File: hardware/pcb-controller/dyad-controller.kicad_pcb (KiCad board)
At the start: 2 copper layers, 45.2 x 93.4 mm, 36 parts, among them J1 USB_C_Receptacle_USB2.0, J2 SWD, J3 Conn_01x11, J4 Conn_01x11, J5 Conn_01x11, SW1 SW_Push, U1 W25Q128JVS, U2 USBLC6-2SC6, U3 RP2040, U4 XC6206PxxxMR-Regulator_Linear, Y1 12MHz

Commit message: Sync the controller PCB with its schematic
The board still carried the upstream reference layout. Cleared its 433
tracks and 32 vias (routed for the 45 x 93 mm board and the old pin map)
and the J3/J4/J5 breakout headers, then added D1, F2, J6-J10 and SW2 from
the schematic, and swapped SW1 from a pin header to the TS-1187A button.

USB-C: the stock USB_C_Receptacle_USB2.0 symbol numbers its shield pin S1,
but KiCad 10's HRO TYPE-C-31-M-12 footprint names those pads SH, so J9/J10
could not be placed with their shield on GND. J1 only worked because it was
the KiCad 6 copy, which still said S1. Added dyad:USB_C_Receptacle_HRO_TYPE-
C-31-M-12 with the shield pads renumbered S1 and pointed J1, J9 and J10 at it.

SW1 fixes: Change Footprint netted only one pad of each duplicate-numbered
pair (the TS-1187A pads are 1,1,2,2), so all four are now netted by hand. It
was also excluded from the BOM -- in the schematic too, inherited from the
header -- which would have left the BOOTSEL button unfitted. Now in_bom yes,
value BOOTSEL.

Verified: 41/41 footprints and 41/41 footprint IDs match the schematic, and
all 246 schematic pins land on correctly netted pads. ERC unchanged at 152.
Parity leaves 14 field-copy differences (LCSC, Datasheet, Serves). The new
parts sit stacked off-board awaiting the 35 x 50 outline and placement.

Co-Authored-By: Claude Opus 5.5 <noreply@anthropic.com>
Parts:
- removed J3, J4, J5: Conn_01x11, Connector_PinSocket_2.54mm:PinSocket_1x11_P2.54mm_Vertical
- added D1: SS34, Diode_SMD:D_SMA, F.Cu at (8.50, 2.38)
- added F2: 500mA, Fuse:Fuse_1206_3216Metric, F.Cu at (7.28, 10.9)
- added J10: USB-C split link, dyad:USB_C_Receptacle_HRO_TYPE-C-31-M-12, F.Cu at (10.3, 70.1)
- added J6: HC-FPC-0.5-20P-FH20, dyad:FPC-SMD_20P-P0.50_HC-FPC-0.5-20P-FH20, F.Cu at (12.4, 20.1)
- added J7: HC-FPC-0.5-20P-FH20, dyad:FPC-SMD_20P-P0.50_HC-FPC-0.5-20P-FH20, F.Cu at (12.4, 31.4)
- added J8: HC-FPC-0.5-14P-FH20, dyad:FPC-SMD_14P-P0.50_HC-FPC-0.5-14P-FH20, F.Cu at (10.9, 42.7)
- added J9: USB-C split link, dyad:USB_C_Receptacle_HRO_TYPE-C-31-M-12, F.Cu at (10.3, 55.7)
- added SW2: RESET, Button_Switch_SMD:SW_Push_1P1T_XKB_TS-1187A, F.Cu at (8.75, 83.3)
- J1: footprint Connector_USB:USB_C_Receptacle_HRO_TYPE-C-31-M-12 -> dyad:USB_C_Receptacle_HRO_TYPE-C-31-M-12
- SW1: value SW_Push -> BOOTSEL; footprint Connector_PinSocket_2.54mm:PinSocket_1x02_P2.54mm_Vertical -> Button_Switch_SMD:SW_Push_1P1T_XKB_TS-1187A
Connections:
- F1 pad 2: +5V -> /VBUS_FUSED
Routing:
- net +3V3: track 75.2 -> 0.00 mm, vias 3 -> 0
- net /GPIO0: track 60.8 -> 0.00 mm
- net /GPIO10: track 57.6 -> 0.00 mm
- net /GPIO1: track 57.4 -> 0.00 mm
- net GND: track 56.8 -> 0.00 mm, vias 25 -> 0
- net /GPIO20: track 54.7 -> 0.00 mm
- net /GPIO11: track 54.3 -> 0.00 mm
- net /GPIO2: track 54.0 -> 0.00 mm
- net /GPIO21: track 52.7 -> 0.00 mm
- net /GPIO22: track 51.7 -> 0.00 mm
- net /GPIO12: track 51.6 -> 0.00 mm
- net /GPIO3: track 50.7 -> 0.00 mm
- net /GPIO23: track 49.7 -> 0.00 mm
- net /GPIO13: track 49.1 -> 0.00 mm
- net /GPIO24: track 47.6 -> 0.00 mm
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
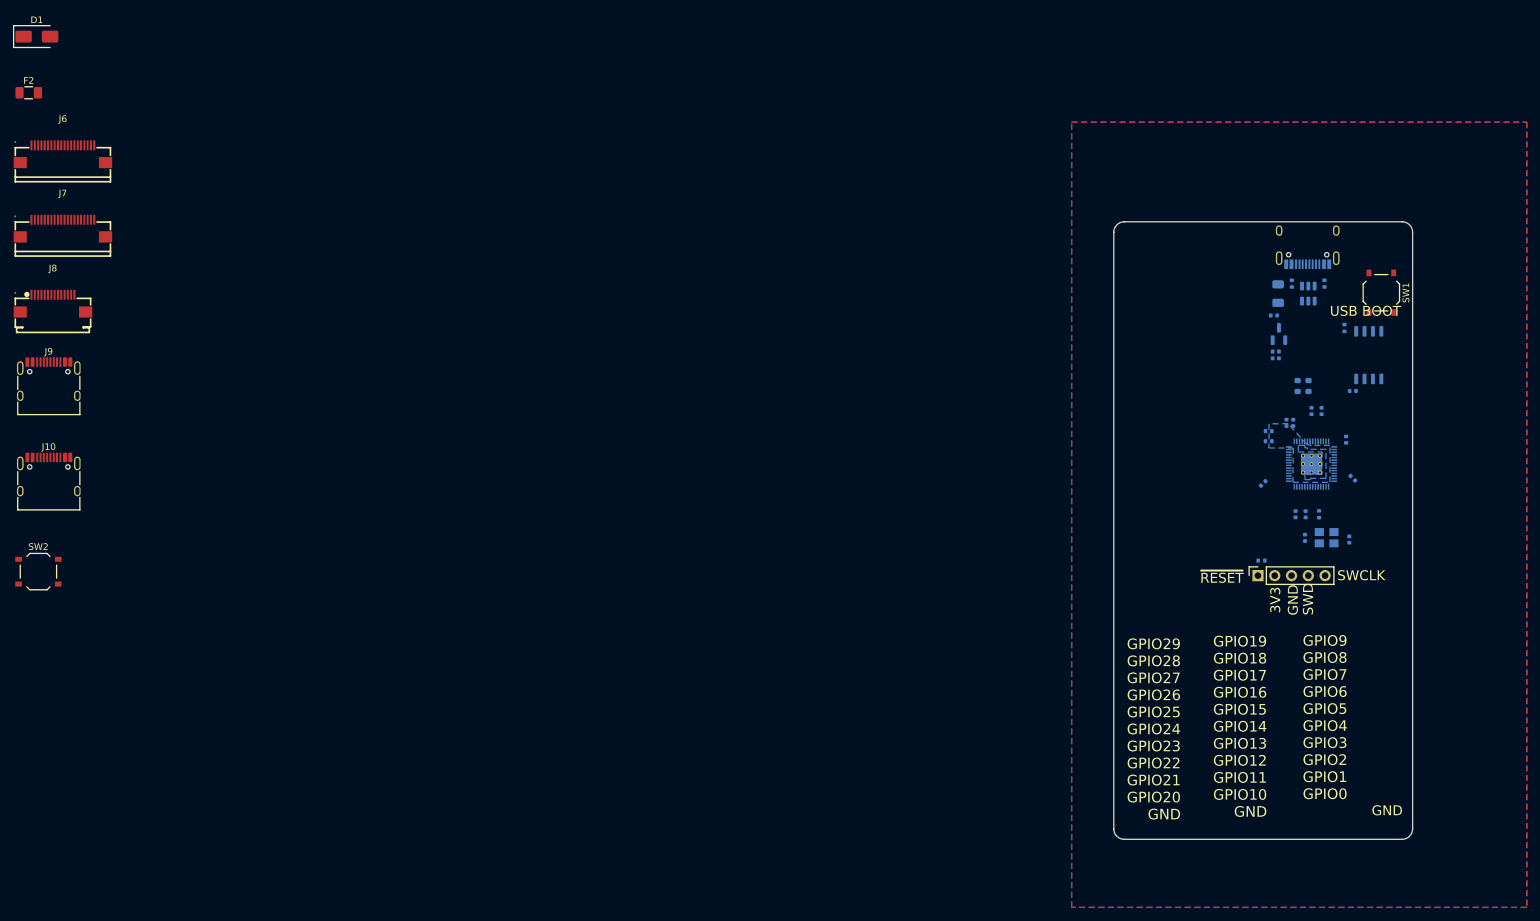
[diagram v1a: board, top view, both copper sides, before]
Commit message: Turn the controller outline to 35 x 50, place the edge connectors and M2 mounting holes
Outline: the upstream 45 x 93 mm shape replaced with 35 wide x 50 deep,
2 mm corners -- the interface.yaml envelope turned 90 degrees so the 50 mm
side edges carry the main FFC and split USB-C. Drawn around the existing
RP2040 so the upstream decoupling cluster stays where it is. The case DXF
and generate_controller_outline.py follow.

Edge connectors, all on B.Cu: J1 host USB-C on the rear; J6/J7 main FFC on
the left/right edges level with U3; J10/J9 split USB-C in front of them; J8
knob FFC front-left. Checked from pad geometry, not angles: every part
opens toward its edge, J6 pad 1 is at the front, J7 pad 1 at the rear and
J8 pin 1 on the right -- the directions the pin map was derived from. FFC
fronts sit 0.2 mm inside the edge; USB-C keeps upstream J1's overhang.

Mounting: four M2 holes (2.2 mm plated, 4.4 mm pad on GND), 3 mm in from
each edge, board-only. M2 because an M3 head at the front-left corner lands
on J8; J8 moved 1.5 mm right for clearance (1.39 mm to the ring). The BOM
and position-file exclusions that Konnect's placement dropped are restored.

interface.yaml v12 records the orientation, the M2 insert and the four
hole positions, which clears controller_envelope.mounting_holes as a G2
blocker. Which face mounts up stays open with standoff_height.

Remaining DRC near these parts is upstream leftovers: the old GND fill and
the Pico breakout's pin-label silkscreen.

Co-Authored-By: Claude Opus 5.5 <noreply@anthropic.com>
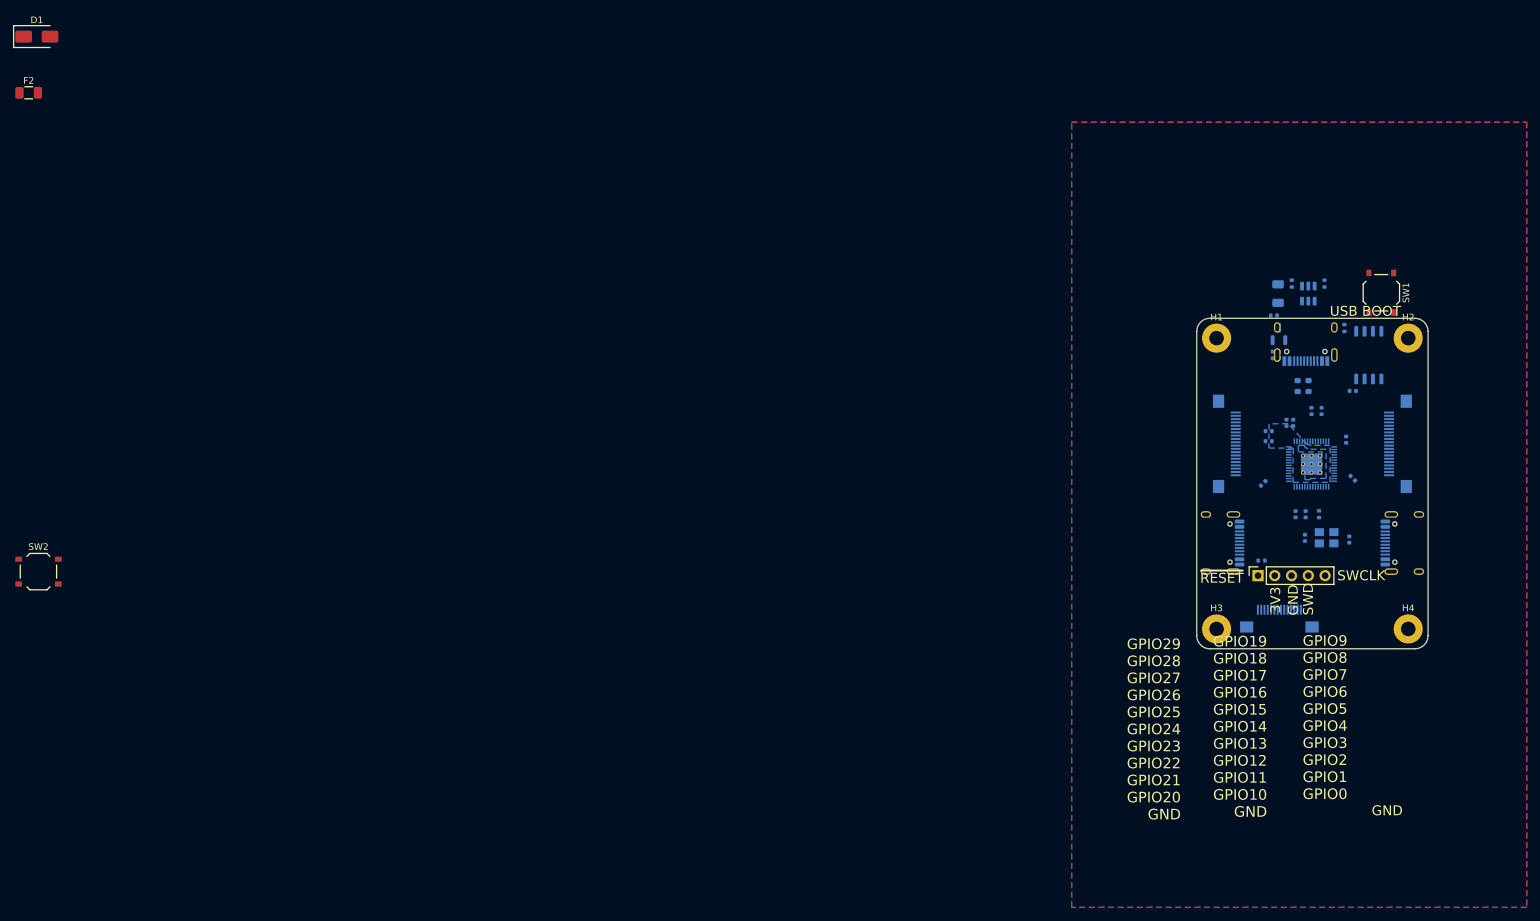
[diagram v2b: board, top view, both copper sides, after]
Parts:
- added H1: MountingHole_2.2mm_M2_Pad, MountingHole:MountingHole_2.2mm_M2_Pad, F.Cu at (187.0, 48.0)
- added H2: MountingHole_2.2mm_M2_Pad, MountingHole:MountingHole_2.2mm_M2_Pad, F.Cu at (216.0, 48.0)
- added H3: MountingHole_2.2mm_M2_Pad, MountingHole:MountingHole_2.2mm_M2_Pad, F.Cu at (187.0, 92.0)
- added H4: MountingHole_2.2mm_M2_Pad, MountingHole:MountingHole_2.2mm_M2_Pad, F.Cu at (216.0, 92.0)
- J10, J6, J7, J8, J9: moved to B.Cu
- moved J9 207.6 mm to (216.6, 79.0), turned to -90 degrees
- moved J7 204.6 mm to (214.4, 64.0), turned to -90 degrees
- moved J8 191.6 mm to (196.5, 90.4), turned to 180 degrees
- moved J6 181.5 mm to (188.6, 64.0), turned to 90 degrees
- moved J10 176.3 mm to (186.4, 79.0), turned to 90 degrees
- moved J1 14.7 mm to (200.5, 47.4)
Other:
- board size 45.2 x 93.4 mm -> 35 x 50 mm

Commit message: Place the controller's remaining parts and clear the upstream leftovers
Every part is now on B.Cu inside the 35 x 50 outline, which leaves F.Cu
free of components so the matrix bundle can cross under the parts.

- MCU block: U3 with all its upstream decoupling, crystal and loading caps
  moved 3 mm forward as a rigid group -- nothing redistributed.
- USB: straight column J1 -> ESD U2 -> R5/R6 -> U3 D+/D-, CC resistors
  R3/R4 beside U2.
- Rear-right: OR-ing D1, F1 by J1's VBUS pins, flash U1 by U3's QSPI side
  with R1 between.
- Rear-left: LDO U4 with C16/C7/C17, BOOTSEL SW1.
- Front-right: SWD header J2, RESET SW2 with R2. Front-left: split fuse F2.
- D1, F2, SW1, SW2 and J2 flipped to B.Cu.

Removed the upstream copper fills (GND, +1V1, +3V3), which now lay across
the new placement, and the Pico breakout's pin-label silkscreen on both
sides. Kept the JLCJLCJLCJLC order-number marker, to be repositioned.

DRC: no courtyard overlaps, edge/hole clearance, shorts or part-to-part
clearance. 78 findings remain -- silkscreen crowding and known library-
version differences. 179 unconnected items is the full ratsnest, unrouted.
Parity: 14 field-copy differences only. 45 footprints, no duplicates.

Co-Authored-By: Claude Opus 5.5 <noreply@anthropic.com>
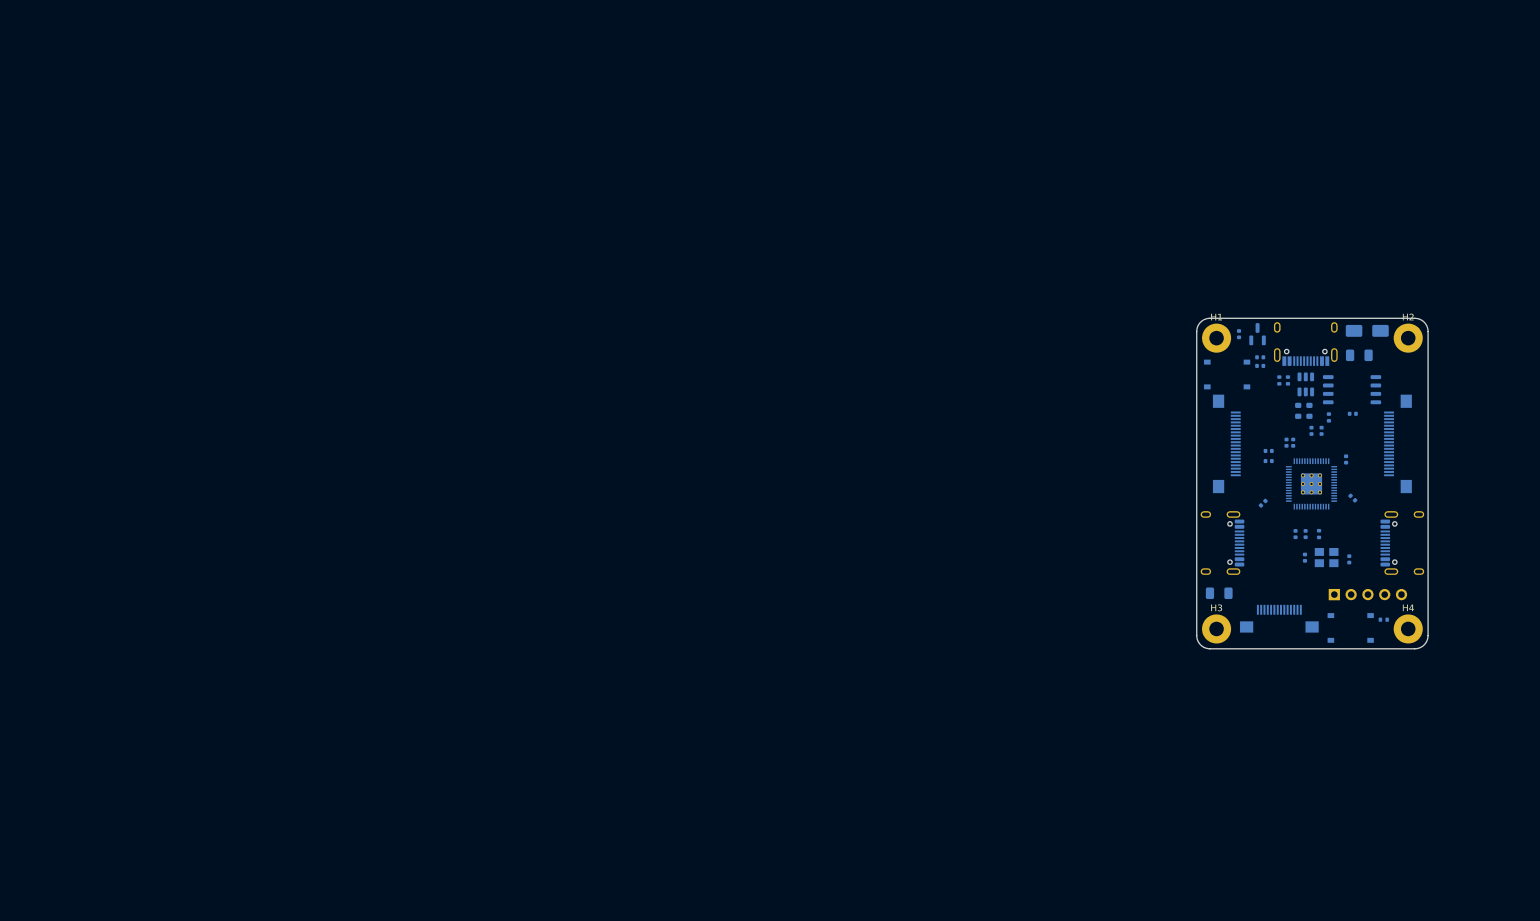
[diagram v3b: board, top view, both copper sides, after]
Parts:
- D1, F2, J2, SW1, SW2: moved to B.Cu
- moved D1 206.2 mm to (209.8, 46.9)
- moved SW2 198.7 mm to (207.3, 91.8)
- moved F2 195.4 mm to (187.4, 86.6)
- moved SW1 26.4 mm to (188.6, 53.5), turned to 180 degrees
- moved R2 20.5 mm to (212.3, 90.6)
- moved R4 16.2 mm to (196.5, 54.4)
- moved F1 15.4 mm to (208.6, 50.6), turned to 0 degrees
- moved R3 14.7 mm to (197.8, 54.4)
- moved U2 13.7 mm to (200.5, 55.0)
- moved R1 13.7 mm to (204.0, 60.0)
- moved J2 11.9 mm to (204.8, 86.8), turned to -90 degrees
- moved C16 5.98 mm to (190.4, 47.4), turned to 90 degrees
- moved U1 5.80 mm to (207.5, 55.8), turned to 0 degrees
- moved R5 3.76 mm to (201.1, 59.0)
- moved R6 3.76 mm to (199.3, 59.0)
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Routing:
- removed copper zone on B.Cu, net +1V1
- removed copper zone on B.Cu, net +3V3
- removed copper zone on B.Cu, net GND
- removed copper zone on F.Cu, net GND
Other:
- board text removed: "3V3"
- board text removed: "GND"
- board text removed: "GPIO19 GPIO18 GPIO17 GPIO16 GPIO15 GPIO14 GPIO13 GPIO12 GPIO11 GPIO10 GND"
- board text removed: "GPIO29 GPIO28 GPIO27 GPIO26 GPIO25 GPIO24 GPIO23 GPIO22 GPIO21 GPIO20 GND"
- board text removed: "GPIO9 GPIO8 GPIO7 GPIO6 GPIO5 GPIO4 GPIO3 GPIO2 GPIO1 GPIO0"
- board text removed: "SWCLK"
- board text removed: "SWD"
- board text removed: "USB BOOT"
- board text removed: "~{RESET}"
